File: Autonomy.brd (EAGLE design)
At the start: 65 x 56 mm, 5 parts, among them J1 APP_2POS_CONFIG12V_HORIZ, K1 PIN20X2, U1 OKI-78SR-5/1.5-W36HC

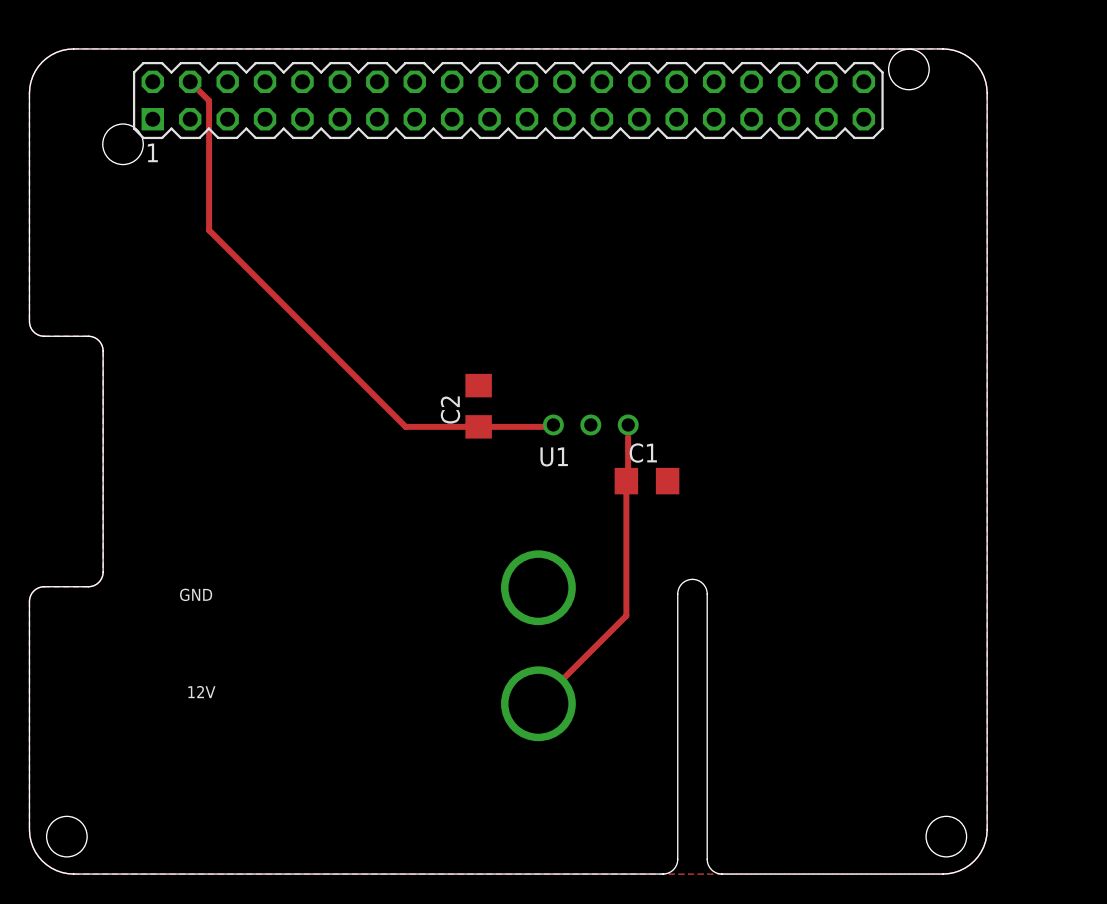
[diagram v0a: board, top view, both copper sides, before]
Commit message: Cleaned up board, added power LED and board label
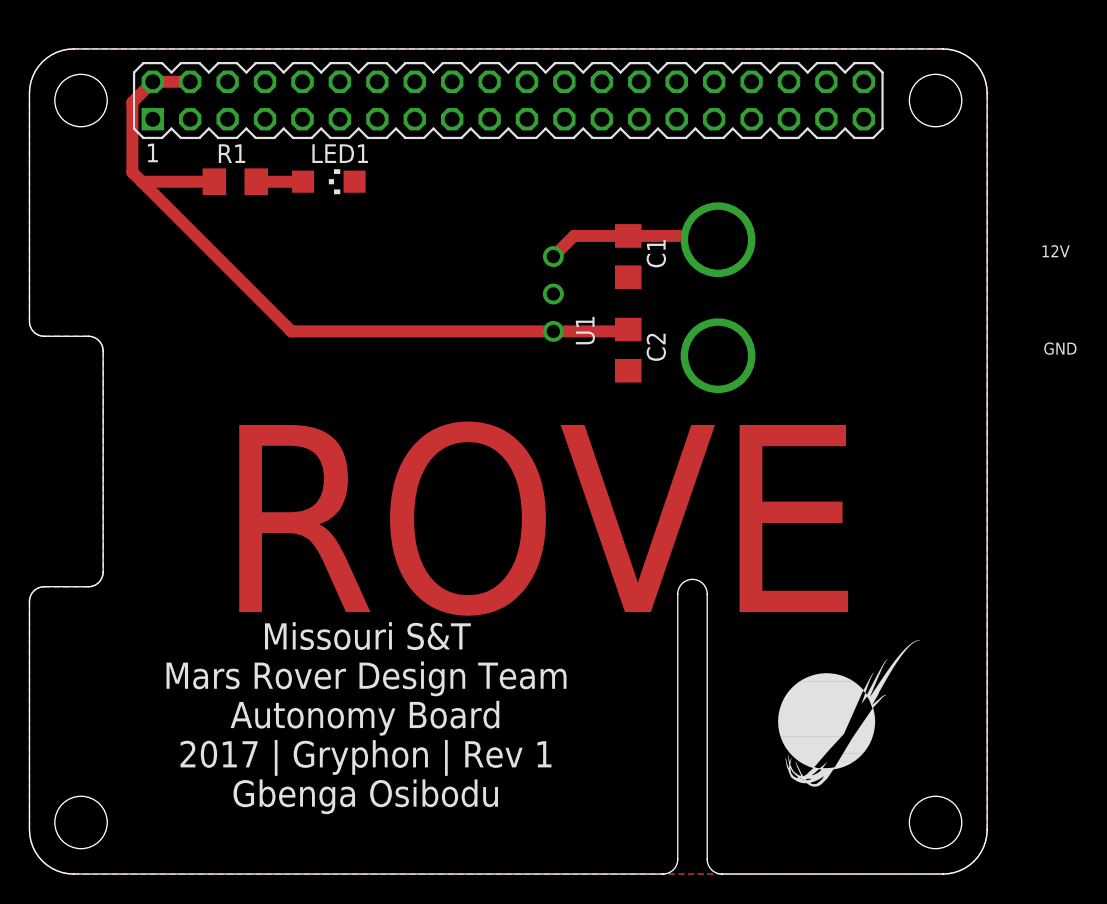
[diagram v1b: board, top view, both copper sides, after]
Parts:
- added LED1: (no value), led:CHIPLED_1206
- added R1: 330, rcl:R1206
- added U$1, U$2, U$3, U$4: (no value), MRDT-Hardware:#6_SCREW
- added U$5: (no value), MRDT-Hardware:MRDT_LOGO
- C1, C2: value (none) -> 10uF
- moved J1 79.1 mm to (74.9, 47.0), turned to 180 degrees
- moved C1 15.3 mm to (40.6, 41.9), turned to 270 degrees
- moved U1 12.5 mm to (35.6, 41.9), turned to 90 degrees
- moved C2 10.9 mm to (40.6, 35.6), turned to 270 degrees
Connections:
- new net N$1: LED1.A, R1.2
- net +5V: now also R1.1
- net GND: now also LED1.C
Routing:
- net +5V: track 39.6 -> 52.4 mm
- net +12V: track 21.4 -> 11.9 mm
- net N$1: track 0.00 -> 3.18 mm
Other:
- board text added: "Missouri S&T Mars Rover Design Team Autonomy Board 2017 | Gryphon | Rev 1 Gbenga Osibodu"
- board text added: "ROVE"
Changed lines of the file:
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@@
 <?xml version="1.0" encoding="utf-8"?>
 <!DOCTYPE eagle SYSTEM "eagle.dtd">
-<eagle version="7.4.0">
+<eagle version="7.5.0">
 <drawing>
 <settings>
@@
 <setting verticaltext="up"/>
 </settings>
-<grid distance="0.05" unitdist="inch" unit="inch" style="lines" multiple="1" display="yes" altdistance="0.000000123031" altunitdist="inch" altunit="inch"/>
+<grid distance="0.05" unitdist="inch" unit="inch" style="lines" multiple="1" display="yes" altdistance="0.025" altunitdist="inch" altunit="inch"/>
 <layers>
 <layer number="1" name="Top" color="4" fill="1" visible="yes" active="yes"/>
@@
 <wire x1="44" y1="1" x2="43" y2="0" width="0" layer="20" curve="-90"/>
 <wire x1="46" y1="1" x2="47" y2="0" width="0" layer="20" curve="90"/>
-<hole x="2.54" y="2.54" drill="2.75"/>
-<hole x="62.23" y="2.54" drill="2.75"/>
-<hole x="59.69" y="54.61" drill="2.75"/>
-<hole x="6.35" y="49.53" drill="2.75"/>
+<text x="22.86" y="10.795" size="1.778" layer="21" font="vector" align="center">Missouri S&amp;T
+Mars Rover Design Team
+Autonomy Board
+2017 | Gryphon | Rev 1
+Gbenga Osibodu</text>
+<text x="12.7" y="17.78" size="12.7" layer="1">ROVE</text>
 </plain>
 <attributes>
@@
 <attribute name="VALUE" x="45.2" y="48.309" size="1.27" layer="27" ratio="10"/>
 </element>
-<element name="J1" library="MRDT-Connectors" package="APP45_12V_HORIZ_CONFIG" value="APP_2POS_CONFIG12V_HORIZ" x="6.35" y="7.62">
-<attribute name="COLOR1" value="YELLOW" x="6.35" y="7.62" size="1.778" layer="27" display="off"/>
-<attribute name="COLOR2" value="BLACK" x="6.35" y="7.62" size="1.778" layer="27" display="off"/>
+<element name="J1" library="MRDT-Connectors" package="APP45_12V_HORIZ_CONFIG" value="APP_2POS_CONFIG12V_HORIZ" x="74.93" y="46.99" rot="R180">
+<attribute name="COLOR1" value="YELLOW" x="74.93" y="46.99" size="1.778" layer="27" rot="R180" display="off"/>
+<attribute name="COLOR2" value="BLACK" x="74.93" y="46.99" size="1.778" layer="27" rot="R180" display="off"/>
 </element>
-<element name="U1" library="MRDT-ICs" package="OKI-78SR_HORIZ" value="OKI-78SR-5/1.5-W36HC" x="40.64" y="30.48">
-<attribute name="VOUT" value="+5v" x="40.64" y="30.48" size="1.778" layer="27" display="off"/>
+<element name="U1" library="MRDT-ICs" package="OKI-78SR_HORIZ" value="OKI-78SR-5/1.5-W36HC" x="35.56" y="41.91" rot="R90">
+<attribute name="VOUT" value="+5v" x="35.56" y="41.91" size="1.778" layer="27" rot="R90" display="off"/>
 </element>
-<element name="C1" library="rcl" package="C1206" value="" x="41.91" y="26.67"/>
-<element name="C2" library="rcl" package="C1206" value="" x="30.48" y="31.75" rot="R90"/>
+<element name="C1" library="rcl" package="C1206" value="10uF" x="40.64" y="41.91" rot="R270"/>
+<element name="C2" library="rcl" package="C1206" value="10uF" x="40.64" y="35.56" rot="R270"/>
+<element name="U$1" library="MRDT-Hardware" package="#6_SCREW" value="" x="3.5" y="52.5"/>
+<element name="U$2" library="MRDT-Hardware" package="#6_SCREW" value="" x="61.5" y="52.5"/>
+<element name="U$3" library="MRDT-Hardware" package="#6_SCREW" value="" x="61.5" y="3.5"/>
+<element name="U$4" library="MRDT-Hardware" package="#6_SCREW" value="" x="3.5" y="3.5"/>
+<element name="U$5" library="MRDT-Hardware" package="MRDT_LOGO" value="" x="50.8" y="5.08"/>
+<element name="LED1" library="led" package="CHIPLED_1206" value="" x="20.32" y="46.99" rot="R270"/>
+<element name="R1" library="rcl" package="R1206" value="330" x="13.97" y="46.99"/>
 </elements>
 <signals>
@@
 <contactref element="C1" pad="2"/>
 <contactref element="C2" pad="2"/>
+<contactref element="LED1" pad="C"/>
 </signal>
 <signal name="+3V3">
@@
 <contactref element="U1" pad="3"/>
 <contactref element="C2" pad="1"/>
-<wire x1="35.56" y1="30.48" x2="35.43" y2="30.35" width="0.4064" layer="1"/>
-<wire x1="35.43" y1="30.35" x2="30.48" y2="30.35" width="0.4064" layer="1"/>
-<wire x1="30.48" y1="30.35" x2="25.53" y2="30.35" width="0.4064" layer="1"/>
-<wire x1="25.53" y1="30.35" x2="12.189778125" y2="43.690221875" width="0.4064" layer="1"/>
-<wire x1="12.189778125" y1="43.690221875" x2="12.189778125" y2="52.490221875" width="0.4064" layer="1"/>
-<wire x1="12.189778125" y1="52.490221875" x2="10.91" y2="53.77" width="0.4064" layer="1"/>
-<wire x1="10.91" y1="53.77" x2="8.37" y2="53.77" width="0" layer="19" extent="1-1"/>
+<wire x1="6.985" y1="47.625" x2="7.62" y2="46.99" width="0.8128" layer="1"/>
+<wire x1="7.62" y1="46.99" x2="17.78" y2="36.83" width="0.8128" layer="1"/>
+<wire x1="17.78" y1="36.83" x2="35.56" y2="36.83" width="0.8128" layer="1"/>
+<wire x1="8.37" y1="53.77" x2="6.985" y2="52.385" width="0.8128" layer="1"/>
+<wire x1="6.985" y1="52.385" x2="6.985" y2="47.625" width="0.8128" layer="1"/>
+<wire x1="8.37" y1="53.77" x2="10.91" y2="53.77" width="0.8128" layer="1"/>
+<wire x1="35.56" y1="36.83" x2="40.51" y2="36.83" width="0.8128" layer="1"/>
+<wire x1="40.51" y1="36.83" x2="40.64" y2="36.96" width="0.8128" layer="1"/>
+<contactref element="R1" pad="1"/>
+<wire x1="12.548" y1="46.99" x2="7.62" y2="46.99" width="0.8128" layer="1"/>
 </signal>
 <signal name="+12V">
@@
 <contactref element="J1" pad="12V"/>
 <contactref element="C1" pad="1"/>
-<wire x1="34.544" y1="11.557" x2="40.51" y2="17.523" width="0.4064" layer="1"/>
-<wire x1="40.51" y1="17.523" x2="40.51" y2="26.67" width="0.4064" layer="1"/>
-<wire x1="40.51" y1="26.67" x2="40.64" y2="26.8" width="0.4064" layer="1"/>
-<wire x1="40.64" y1="26.8" x2="40.64" y2="30.48" width="0.4064" layer="1"/>
+<wire x1="40.64" y1="43.31" x2="36.96" y2="43.31" width="0.8128" layer="1"/>
+<wire x1="36.96" y1="43.31" x2="35.56" y2="41.91" width="0.8128" layer="1"/>
+<wire x1="40.64" y1="43.31" x2="46.479" y2="43.31" width="0.8128" layer="1"/>
+<wire x1="46.479" y1="43.31" x2="46.736" y2="43.053" width="0.8128" layer="1"/>
+</signal>
+<signal name="N$1">
+<contactref element="LED1" pad="A"/>
+<contactref element="R1" pad="2"/>
+<wire x1="15.392" y1="46.99" x2="18.57" y2="46.99" width="0.8128" layer="1"/>
 </signal>
 </signals>
@@
 </board>
 </drawing>
+<compatibility>
+<note version="6.3" minversion="6.2.2" severity="warning">
+Since Version 6.2.2 text objects can contain more than one line,
+which will not be processed correctly with this version.
+</note>
+</compatibility>
 </eagle>

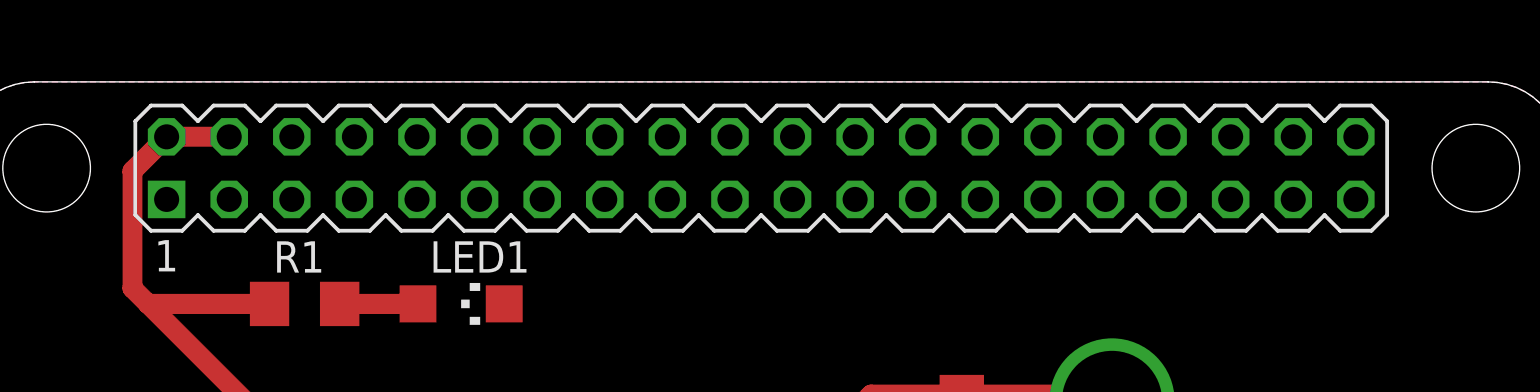
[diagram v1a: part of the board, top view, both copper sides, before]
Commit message: Removed unnecessary 3v3 net and swapped header with eagle standard part
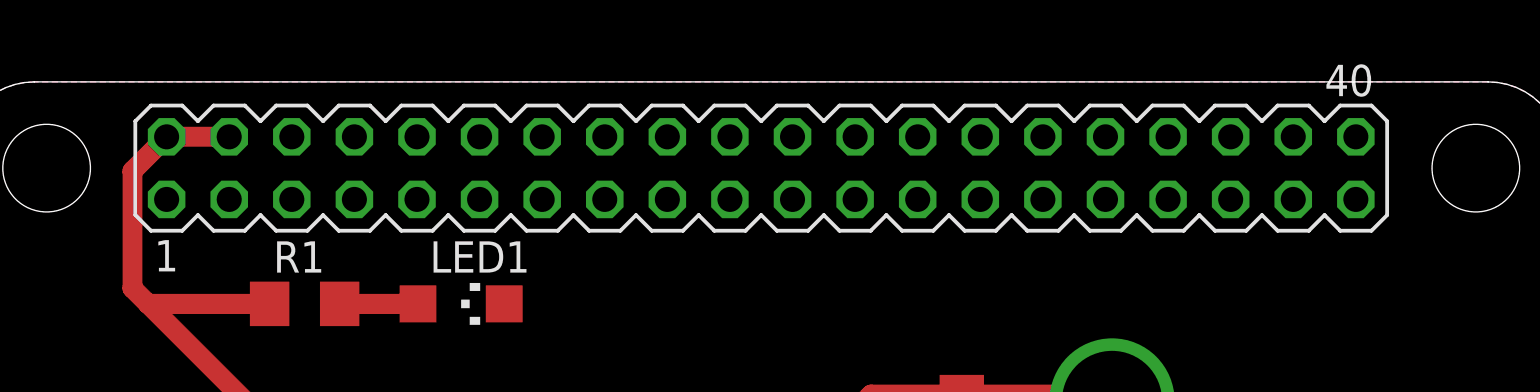
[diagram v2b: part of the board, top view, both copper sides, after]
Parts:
- K1: value PIN20X2 -> (none); device FLYFISH:PIN_20X2 -> con-lstb:MA20-2
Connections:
- removed net +3V3: K1.1, K1.17
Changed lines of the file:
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@@
 <setting verticaltext="up"/>
 </settings>
-<grid distance="0.05" unitdist="inch" unit="inch" style="lines" multiple="1" display="yes" altdistance="0.025" altunitdist="inch" altunit="inch"/>
+<grid distance="1" unitdist="mm" unit="mm" style="lines" multiple="1" display="yes" altdistance="0.025" altunitdist="inch" altunit="inch"/>
 <layers>
 <layer number="1" name="Top" color="4" fill="1" visible="yes" active="yes"/>
@@
 </autorouter>
 <elements>
-<element name="K1" library="FLYFISH" package="PIN_20X2" value="PIN20X2" x="32.5" y="52.5" smashed="yes">
+<element name="K1" library="con-lstb" package="MA20-2" value="" x="32.5" y="52.5" smashed="yes">
 <attribute name="VALUE" x="45.2" y="48.309" size="1.27" layer="27" ratio="10"/>
+<attribute name="MPN" value="" x="32.5" y="52.5" size="1.778" layer="27" display="off"/>
+<attribute name="OC_NEWARK" value="unknown" x="32.5" y="52.5" size="1.778" layer="27" display="off"/>
+<attribute name="OC_FARNELL" value="unknown" x="32.5" y="52.5" size="1.778" layer="27" display="off"/>
+<attribute name="MF" value="" x="32.5" y="52.5" size="1.778" layer="27" display="off"/>
 </element>
 <element name="J1" library="MRDT-Connectors" package="APP45_12V_HORIZ_CONFIG" value="APP_2POS_CONFIG12V_HORIZ" x="74.93" y="46.99" rot="R180">
@@
 <contactref element="LED1" pad="C"/>
 </signal>
-<signal name="+3V3">
-<contactref element="K1" pad="1"/>
-<contactref element="K1" pad="17"/>
-<wire x1="8.37" y1="51.23" x2="28.69" y2="51.23" width="0" layer="19" extent="1-1"/>
-</signal>
 <signal name="+5V">
